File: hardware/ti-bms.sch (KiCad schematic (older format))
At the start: 64 parts, among them J1 Conn_02x03_Odd_Even, J2 Conn_01x02, J3 Conn_01x02, J4 Conn_01x02, J5 CAN_TERM, U1 Pico, U2 MCP2515-xST, U3 SN65HVD231, U4 TPS62160DGK, U5 MAX3485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

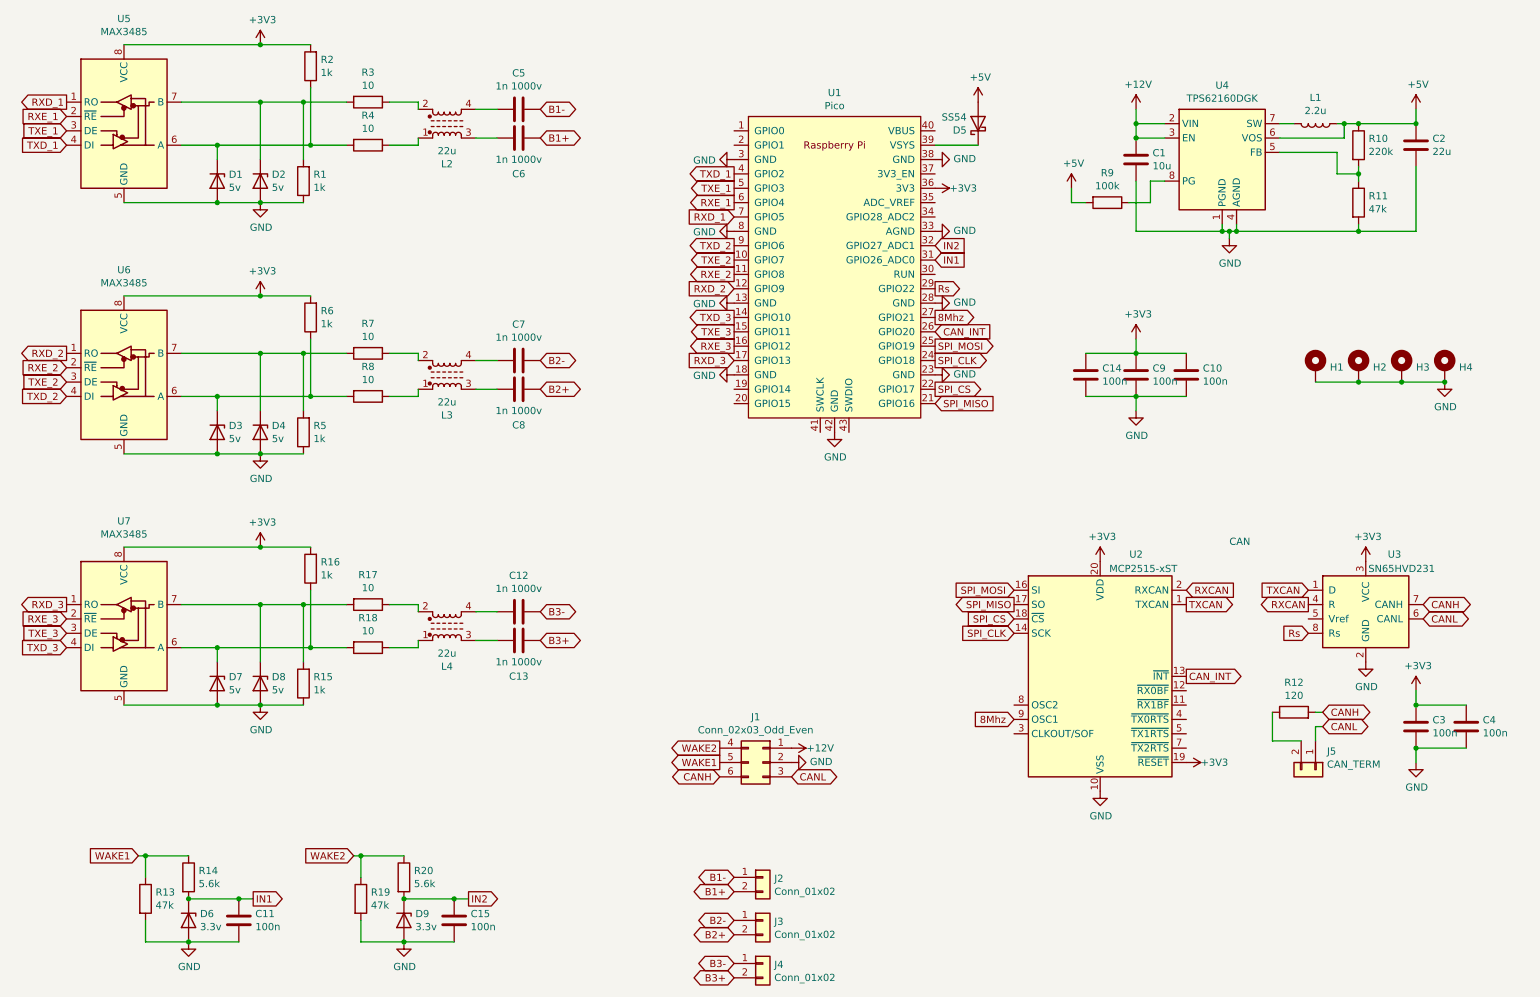
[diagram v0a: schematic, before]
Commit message: v4 hardware with 5v line drivers
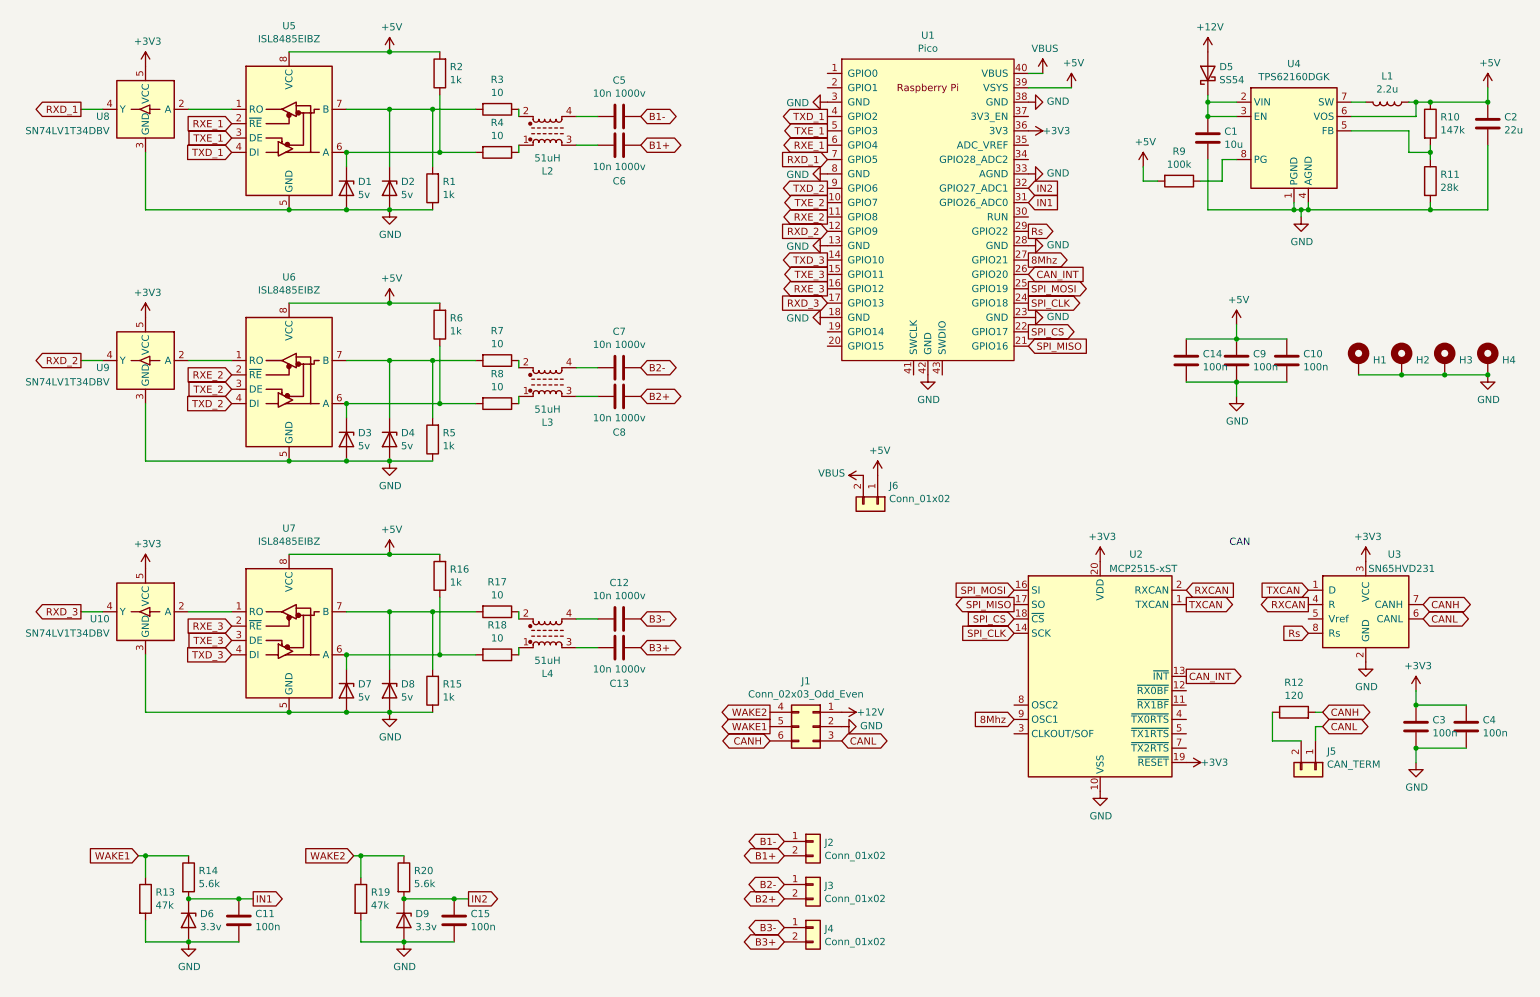
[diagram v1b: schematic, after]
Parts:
- added J6: Conn_01x02, Connector_PinHeader_2.54mm:PinHeader_1x02_P2.54mm_Vertical, symbol Connector_Generic:Conn_01x02
- added U10, U8, U9: SN74LV1T34DBV, Package_TO_SOT_SMD:SOT-23-5, symbol Logic_LevelTranslator:SN74LV1T34DBV
- C12, C13, C5, C6, C7, C8: value 1n 1000v -> 10n 1000v; LCSC C1941 -> C9194
- L2, L3, L4: value 22u -> 51uH; LCSC C88055 -> C76584
- R10: value 220k -> 147k; LCSC C22961 -> C22878
- R11: value 47k -> 28k; LCSC C25819 -> C22989
- U5, U6, U7: value MAX3485 -> ISL8485EIBZ; LCSC C18148 -> C382024
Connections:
- net +12V: now also D5.2 (A); no longer C1.1, U4.2 (VIN), U4.3 (EN)
- net +3V3: now also U10.5 (VCC), U8.5 (VCC), U9.5 (VCC); no longer C10.1, C14.1, C9.1, R16.2, R2.2, R6.2, U5.8 (VCC), U6.8 (VCC), U7.8 (VCC)
- net +5V: now also C10.1, C14.1, C9.1, R16.2, R2.2, R6.2, U1.39 (VSYS), U5.8 (VCC), U6.8 (VCC), U7.8 (VCC), J6.1 (Pin_1); no longer D5.2 (A)
- net GND: now also U10.3 (GND), U8.3 (GND), U9.3 (GND)
- net RXD_1: now also U8.4 (Y); no longer U5.1 (RO)
- net RXD_2: now also U9.4 (Y); no longer U6.1 (RO)
- net RXD_3: now also U10.4 (Y); no longer U7.1 (RO)
- net at D5.1 (K): now also C1.1, U4.2 (VIN), U4.3 (EN); no longer U1.39 (VSYS)
- net VBUS: now reaches U1.40 (VBUS)
- net VBUS: now also J6.2 (Pin_2)
- new net: U5.1 (RO), U8.2 (A)
- new net: U6.1 (RO), U9.2 (A)
- new net: U10.2 (A), U7.1 (RO)
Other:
- moved on the sheet: C1, C10, C12, C13, C14, C2, C5, C6, C7, C8, C9, D1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

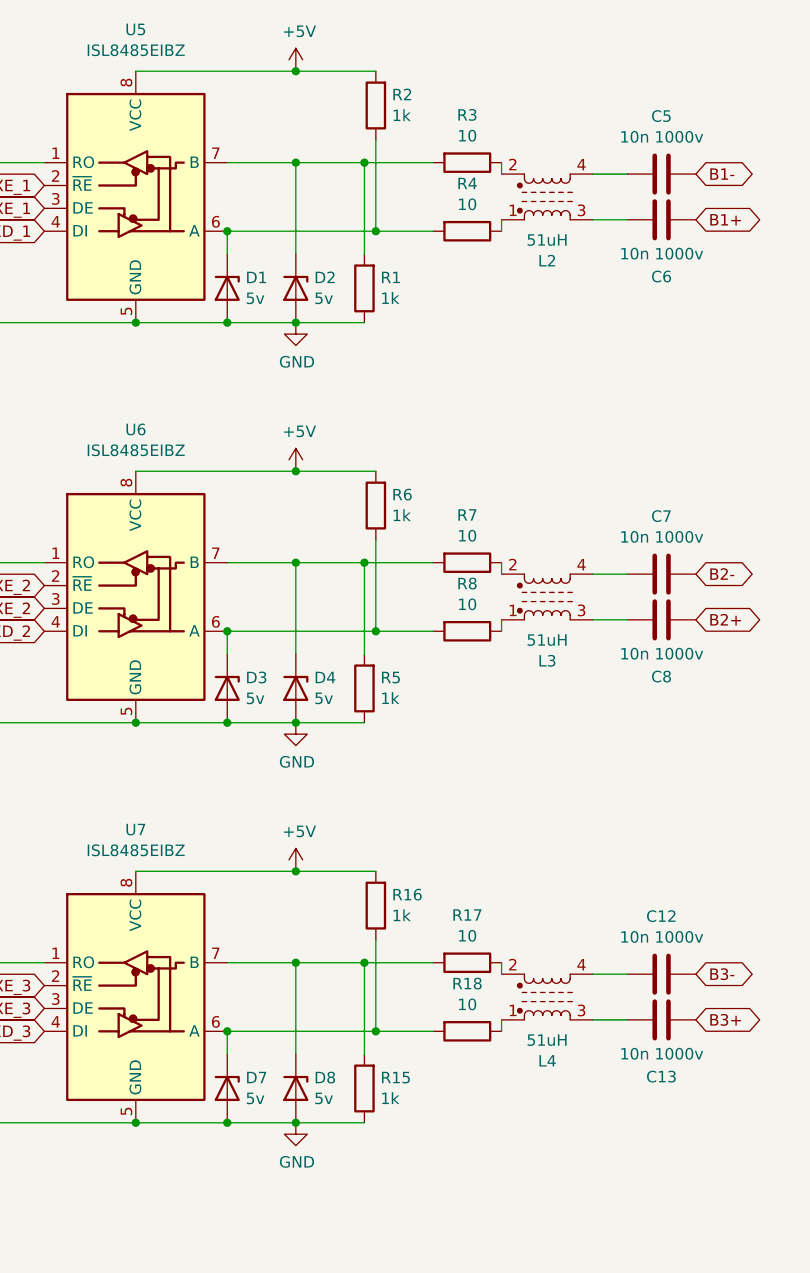
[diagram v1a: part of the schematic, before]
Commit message: change resistor value, better error logging, remove redundant code
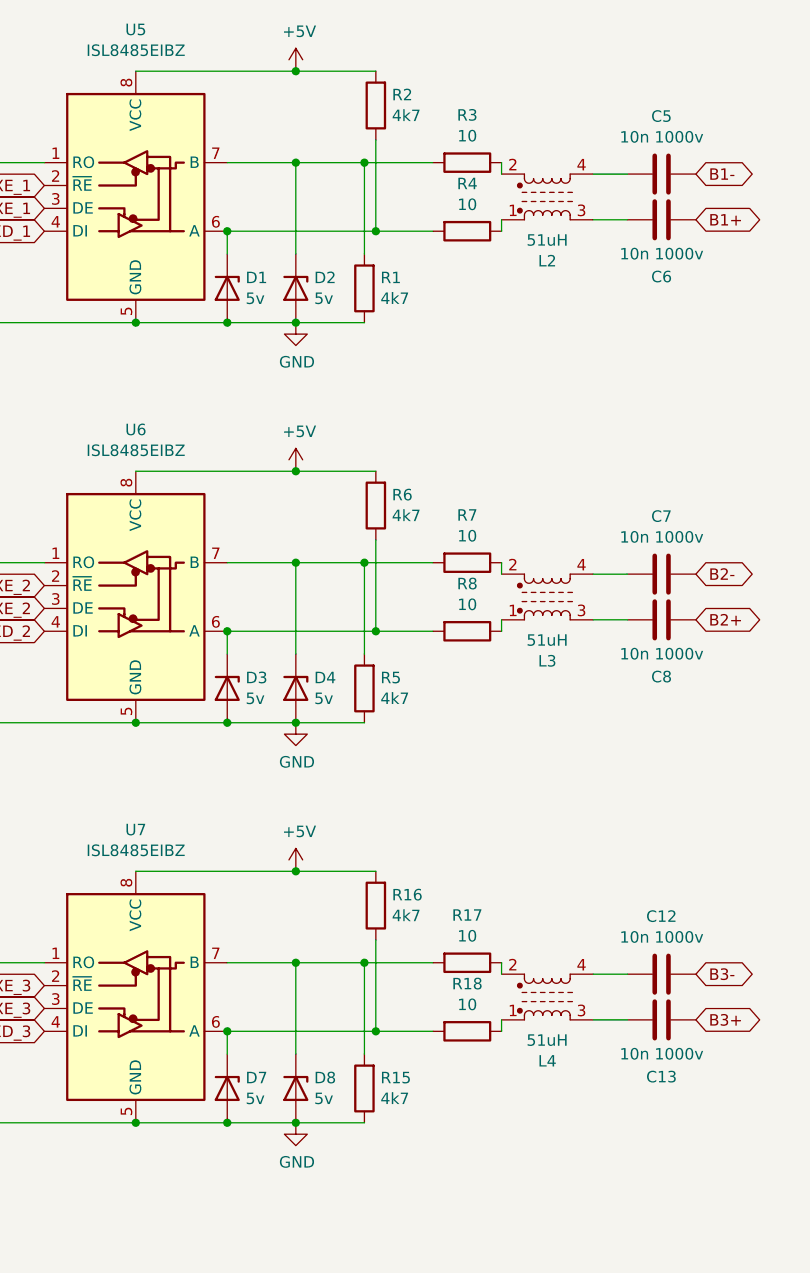
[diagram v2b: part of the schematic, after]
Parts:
- R1, R15, R16, R2, R5, R6: value 1k -> 4k7; LCSC C21190 -> C23162
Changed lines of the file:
@@
 P 3600 1000
 F 0 "R2" H 3530 954 50  0000 R CNN
-F 1 "1k" H 3530 1045 50  0000 R CNN
+F 1 "4k7" H 3530 1045 50  0000 R CNN
 F 2 "Resistor_SMD:R_0603_1608Metric" V 3530 1000 50  0001 C CNN
 F 3 "~" H 3600 1000 50  0001 C CNN
-F 4 "C21190" H 3600 1000 50  0001 C CNN "LCSC"
+F 4 "C23162" H 3600 1000 50  0001 C CNN "LCSC"
 	1    3600 1000
 	-1   0    0    1
@@
 P 3550 1800
 F 0 "R1" H 3480 1754 50  0000 R CNN
-F 1 "1k" H 3480 1845 50  0000 R CNN
+F 1 "4k7" H 3480 1845 50  0000 R CNN
 F 2 "Resistor_SMD:R_0603_1608Metric" V 3480 1800 50  0001 C CNN
 F 3 "~" H 3550 1800 50  0001 C CNN
-F 4 "C21190" H 3550 1800 50  0001 C CNN "LCSC"
+F 4 "C23162" H 3550 1800 50  0001 C CNN "LCSC"
 	1    3550 1800
 	-1   0    0    1
@@
 P 3600 2750
 F 0 "R6" H 3530 2704 50  0000 R CNN
-F 1 "1k" H 3530 2795 50  0000 R CNN
+F 1 "4k7" H 3530 2795 50  0000 R CNN
 F 2 "Resistor_SMD:R_0603_1608Metric" V 3530 2750 50  0001 C CNN
 F 3 "~" H 3600 2750 50  0001 C CNN
-F 4 "C21190" H 3600 2750 50  0001 C CNN "LCSC"
+F 4 "C23162" H 3600 2750 50  0001 C CNN "LCSC"
 	1    3600 2750
 	-1   0    0    1
@@
 P 3550 3550
 F 0 "R5" H 3480 3504 50  0000 R CNN
-F 1 "1k" H 3480 3595 50  0000 R CNN
+F 1 "4k7" H 3480 3595 50  0000 R CNN
 F 2 "Resistor_SMD:R_0603_1608Metric" V 3480 3550 50  0001 C CNN
 F 3 "~" H 3550 3550 50  0001 C CNN
-F 4 "C21190" H 3550 3550 50  0001 C CNN "LCSC"
+F 4 "C23162" H 3550 3550 50  0001 C CNN "LCSC"
 	1    3550 3550
 	-1   0    0    1
@@
 P 3600 4500
 F 0 "R16" H 3530 4454 50  0000 R CNN
-F 1 "1k" H 3530 4545 50  0000 R CNN
+F 1 "4k7" H 3530 4545 50  0000 R CNN
 F 2 "Resistor_SMD:R_0603_1608Metric" V 3530 4500 50  0001 C CNN
 F 3 "~" H 3600 4500 50  0001 C CNN
-F 4 "C21190" H 3600 4500 50  0001 C CNN "LCSC"
+F 4 "C23162" H 3600 4500 50  0001 C CNN "LCSC"
 	1    3600 4500
 	-1   0    0    1
@@
 P 3550 5300
 F 0 "R15" H 3480 5254 50  0000 R CNN
-F 1 "1k" H 3480 5345 50  0000 R CNN
+F 1 "4k7" H 3480 5345 50  0000 R CNN
 F 2 "Resistor_SMD:R_0603_1608Metric" V 3480 5300 50  0001 C CNN
 F 3 "~" H 3550 5300 50  0001 C CNN
-F 4 "C21190" H 3550 5300 50  0001 C CNN "LCSC"
+F 4 "C23162" H 3550 5300 50  0001 C CNN "LCSC"
 	1    3550 5300
 	-1   0    0    1
